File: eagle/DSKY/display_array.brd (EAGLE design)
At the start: 160 x 100 mm, 124 parts, among them IC1001 PCF8574AT, IC101 PCF8574T, IC1201 SN7400N, IC1202 SN7400N, IC1301 SN7400N, IC1302 SN7400N, IC1601 NE555V, IC201 PCF8574T, IC301 PCF8574T, IC401 PCF8574T, IC501 PCF8574T, IC601 PCF8574T, IC701 PCF8574T, IC801 PCF8574T, IC901 PCF8574AT, T1601 NX2301P, T1602 NX2301P, X1401 CLAMP_1X4-T-5MM, X1402 MALE_2X13-T-VERTICAL_2.54MM, X1501 MALE_2X13-T-VERTICAL_2.54MM

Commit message: silk screen for keys fixed
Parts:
- added LED1, LED2: red, be_opt:S_0805
- added R1: 1k5, be_rcl:S_0805
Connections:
- net N$1 renamed DRV_9_LED_R1BB
- net N$2 renamed DRV_9_LED_R1AA
- new net DRV_9_LED_R1C: LED1.C, R1.2
- new net DRV_9_LED_R1CC: LED1.A, LED2.C
- net DRV_9_LED_1: now also R1.1
- net DRV_ANODE_1: now also LED2.A
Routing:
- net DRV_9_LED_1: track 163.9 -> 213.2 mm, vias 0 -> 2
- net DRV_ANODE_1: track 244.4 -> 260.4 mm
- net DRV_9_LED_R1C: track 0.00 -> 9.71 mm
- net DRV_9_LED_R1CC: track 0.00 -> 5.07 mm

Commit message: fixed attributes
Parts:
- removed LED1, LED2: red, be_opt:S_0805
- removed R1: 1k5, be_rcl:S_0805
- added C1604: 10n, be_rcl:S_0805
- added LED912, LED913: red, be_opt:S_0805
- added R910: 2k5, be_rcl:S_0805
- C1602: value 47n -> 100n
- C1603: value 10n -> 100n
- LED903: value green -> red
- LED905: value yellow -> green
- LED907: value red -> yellow
- LED908: value blue -> red
- LED910: value red -> blue
- R903: value 750 -> 1k5
- R905: value 2k2 -> 750
- R907: value 3k3 -> 2k2
- R908: value 2k5 -> 3k3
- moved C1602 71.7 mm to (3.00, -2.00), turned to 0 degrees
- moved R903 61.7 mm to (68.0, 79.0)
- moved LED903 56.5 mm to (68.2, 86.8), turned to 90 degrees
- moved LED901 54.0 mm to (41.1, 86.8)
- moved R901 54.0 mm to (41.0, 79.0)
- moved LED910 31.3 mm to (124.0, 71.0), turned to 270 degrees
- moved LED911 27.0 mm to (41.1, 83.2)
- moved LED902 27.0 mm to (95.2, 86.8)
- moved R902 27.0 mm to (95.0, 79.0)
- moved C1603 14.1 mm to (12.8, 69.0), turned to 180 degrees
- moved R906 8.40 mm to (131.8, 62.2)
- moved LED904 4.00 mm to (124.0, 95.0)
- moved LED905 4.00 mm to (124.0, 91.0)
- moved LED906 4.00 mm to (124.0, 87.0)
- moved LED907 4.00 mm to (124.0, 83.0)
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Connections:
- new net N$1: C1602.2, C1603.1
- net DRV_9_LED_1: now also R903.1; no longer R1.1
- net DRV_9_LED_2: now also R904.1; no longer R903.1
- net DRV_9_LED_3: now also R905.1; no longer R904.1
- net DRV_9_LED_4: now also R906.1; no longer R905.1
- net DRV_9_LED_5: now also R907.1; no longer R906.1
- net DRV_9_LED_6: now also R908.1; no longer R907.1
- net DRV_9_LED_7: now also R909.1; no longer R908.1
- net DRV_9_LED_8: now also R910.1; no longer R909.1
- net DRV_9_LED_R1A: now also LED902.C, R902.2; no longer LED901.C, R901.2
- net DRV_9_LED_R1AA: now also LED902.A, LED912.C; no longer LED901.A, LED910.C
- net DRV_9_LED_R1B: now also LED903.C, R903.2; no longer LED902.C, R902.2
- net DRV_9_LED_R1BB: now also LED903.A, LED913.C; no longer LED902.A, LED911.C
- net DRV_9_LED_R1C: now also LED901.C, R901.2; no longer LED1.C, R1.2
- net DRV_9_LED_R1CC: now also LED901.A, LED911.C; no longer LED1.A, LED2.C
- net DRV_9_LED_R2: now also LED904.C, R904.2; no longer LED903.C, R903.2
- net DRV_9_LED_R3: now also LED905.C, R905.2; no longer LED904.C, R904.2
- net DRV_9_LED_R4: now also LED906.C, R906.2; no longer LED905.C, R905.2
- net DRV_9_LED_R5: now also LED907.C, R907.2; no longer LED906.C, R906.2
- net DRV_9_LED_R6: now also LED908.C, R908.2; no longer LED907.C, R907.2
- net DRV_9_LED_R7: now also LED909.C, R909.2; no longer LED908.C, R908.2
- net DRV_9_LED_R8: now also LED910.C, R910.2; no longer LED909.C, R909.2
- net DRV_ANODE_1: now also LED912.A, LED913.A; no longer LED2.A, LED903.A
- net GND: now also C1604.2; no longer C1602.2
- net TIM_1: now also C1604.1; no longer C1603.1
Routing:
- net TIM_2: track 39.3 -> 31.9 mm

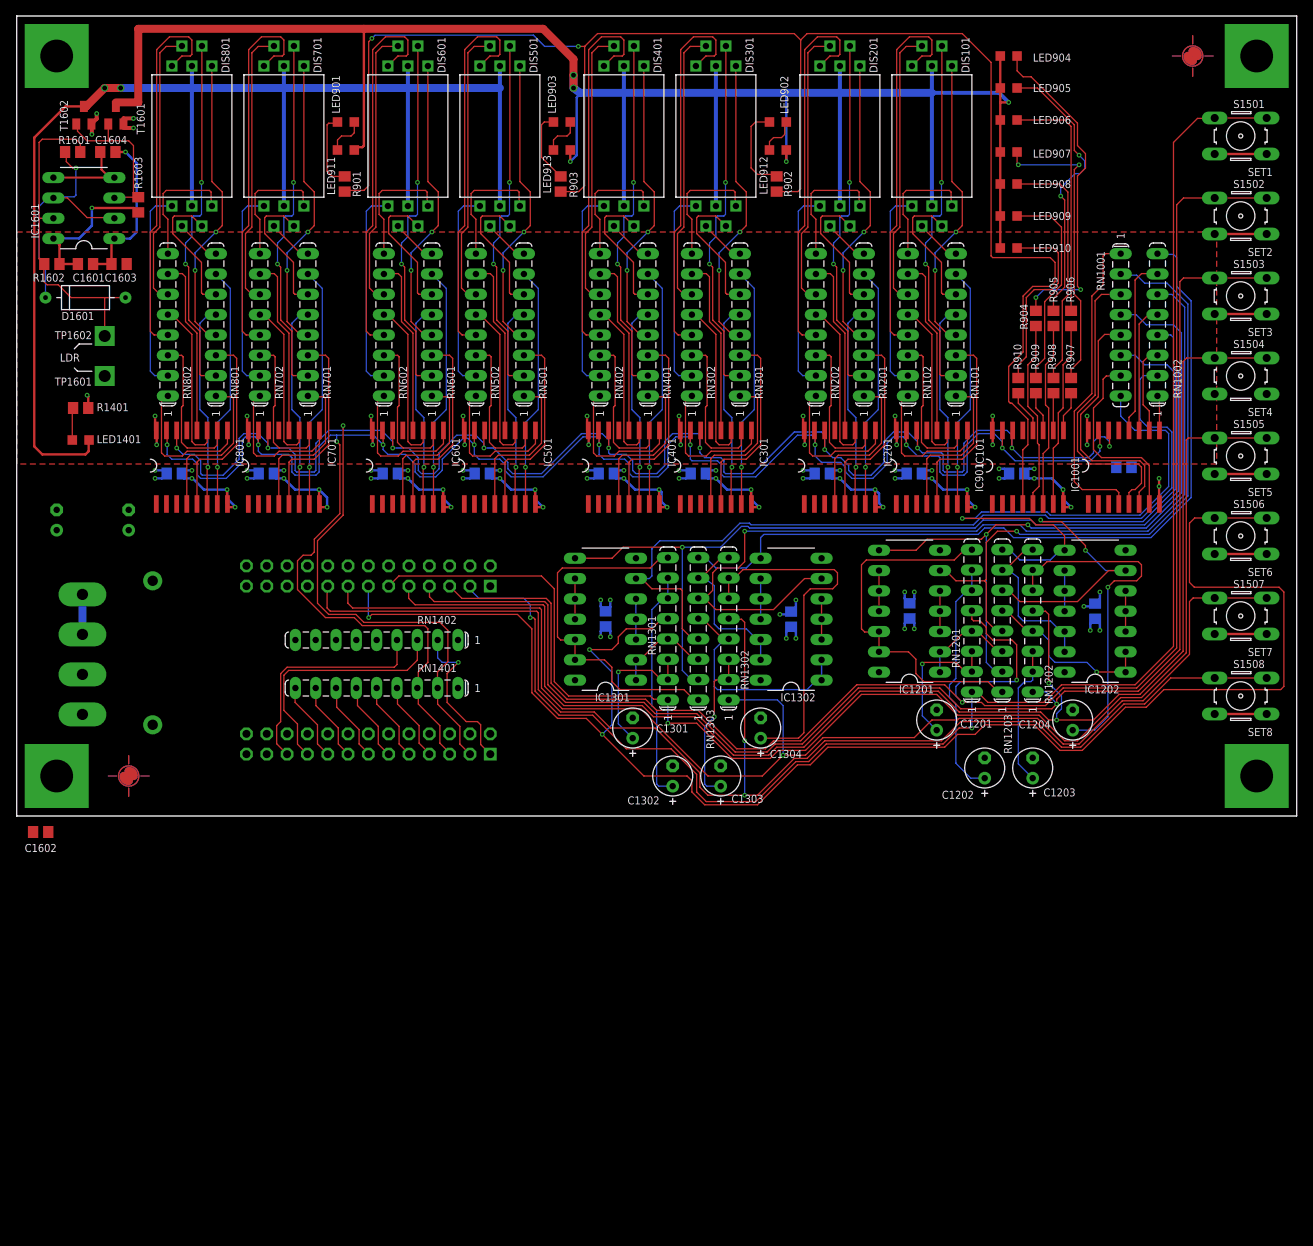
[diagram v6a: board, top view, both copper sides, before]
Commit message: -routed supply -applied dru Q-Print standard
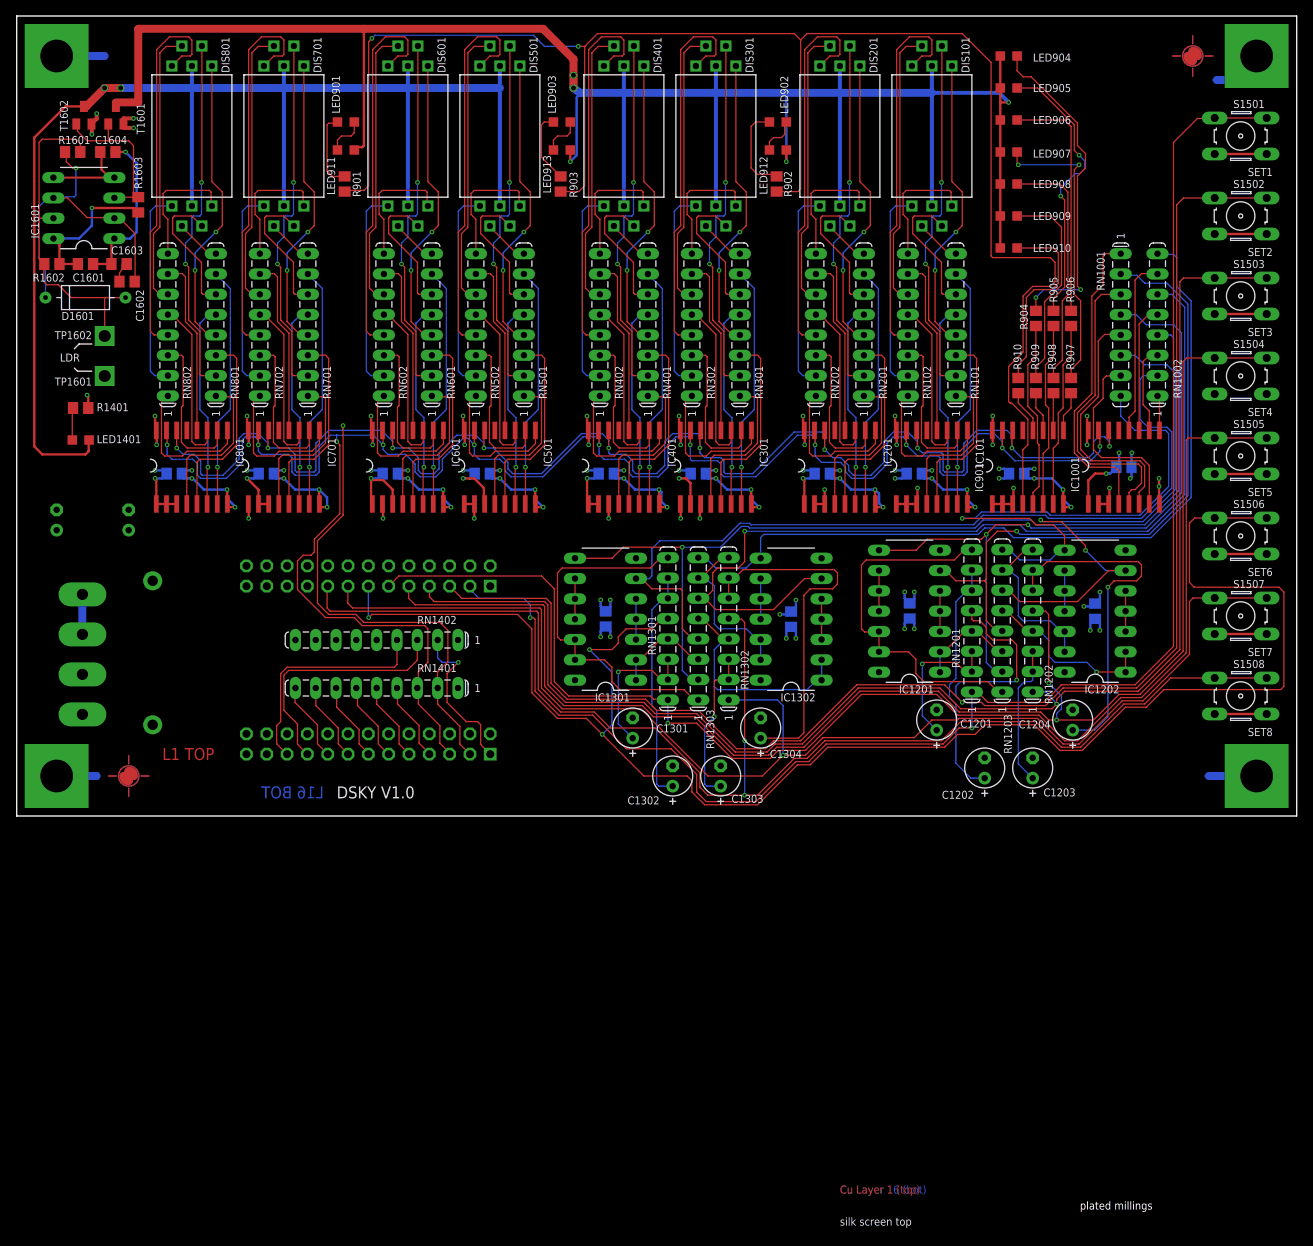
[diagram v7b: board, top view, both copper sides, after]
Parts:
- added U$1: (no value), be_frame:A4_LANDSCAPE
- R909, R910: value 2k5 -> 2k4
- moved C1602 69.6 mm to (13.8, 66.8), turned to 180 degrees
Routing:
- net GND: track 209.6 -> 263.9 mm, vias 48 -> 60
- net P5V: track 111.6 -> 157.3 mm, vias 51 -> 53
- net TIM_2: track 31.9 -> 41.3 mm
- net N$1: track 0.00 -> 2.85 mm
- net KEYPAD_1_K_1: track 39.6 -> 39.1 mm
- added copper zone on layer 15, net GND
- added copper zone on layer 2, net P5V
- removed copper zone on layer 1, net P5V
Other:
- board text added: "DSKY V1.0"
- board text added: "L1 TOP"
- board text added: "L15 GND"
- board text added: "L16 BOT"
- board text added: "L2 P5V"

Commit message: fixed silk screen issues
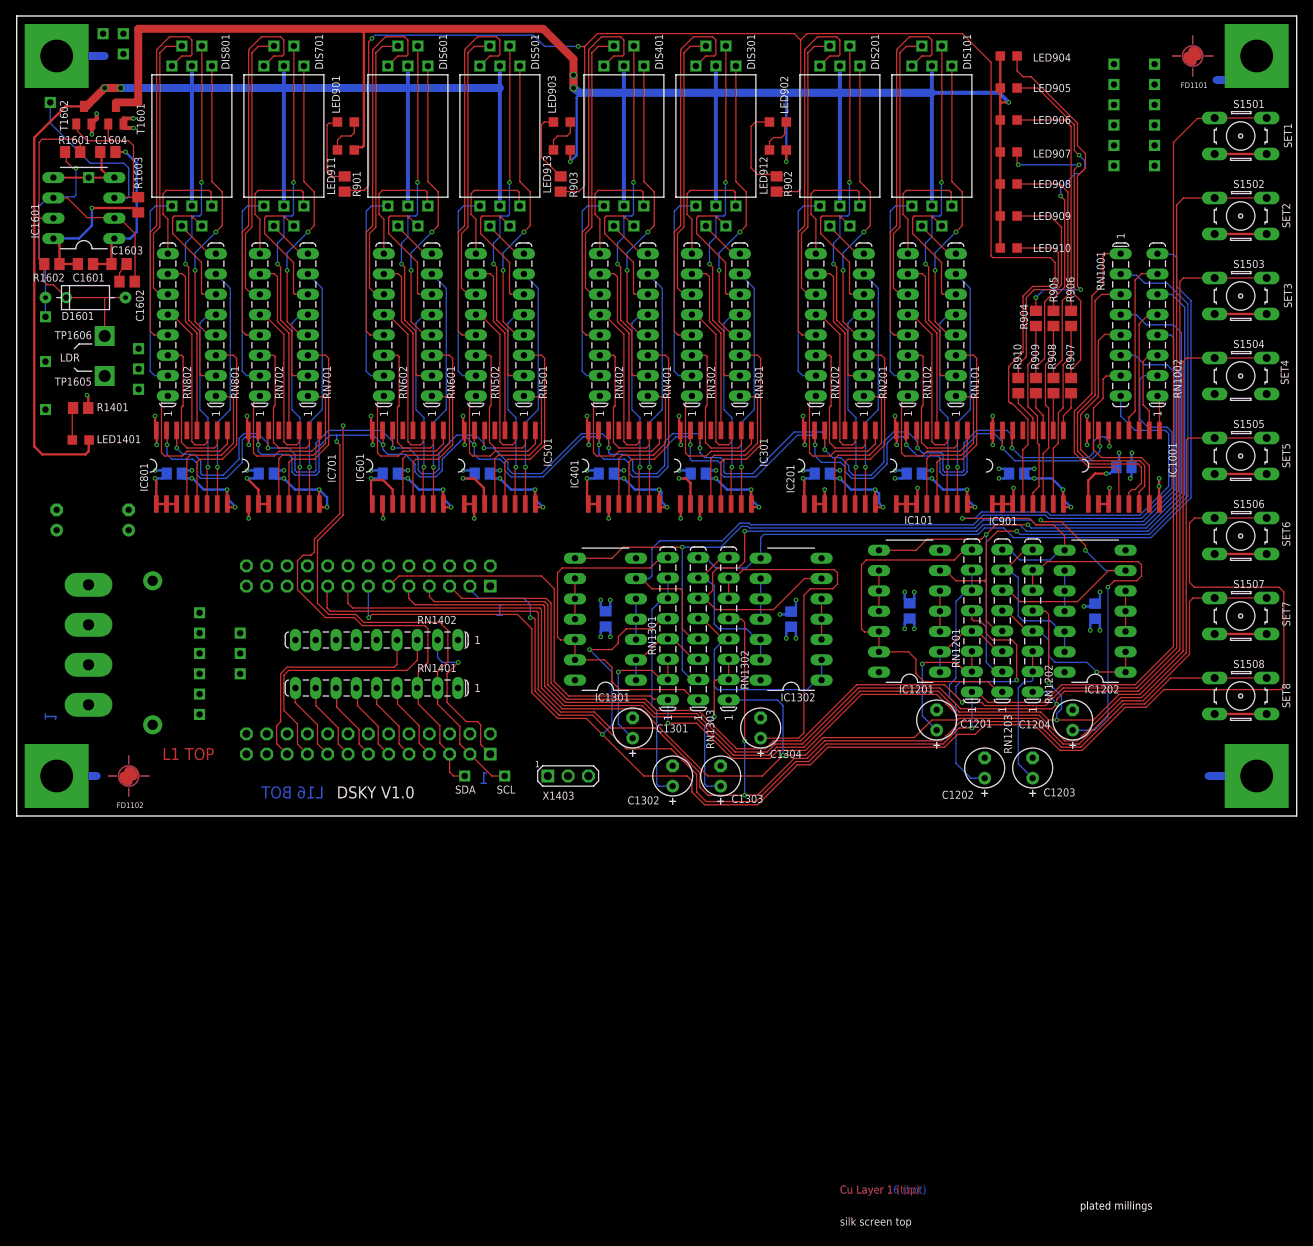
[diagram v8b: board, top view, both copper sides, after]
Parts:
- added TP1101, TP1102, TP1103, TP1104, TP1105, TP1106, TP1107, TP1108, TP1109, TP1110, TP1111, TP1112, TP1113, TP1114, TP1115, TP1116, TP1117, TP1118, TP1119, TP1120, TP1121, TP1122, TP1123, TP1124, TP1125, TP1126, TP1127, TP1401, TP1402, TP1603, TP1604, TP1607: TEST_POINT_T_SMALL, be_con_jump:T_TEST_POINT_SMALL
- added TP1605, TP1606: TEST_POINT_T_LARGE, be_con_jump:T_TEST_POINT_LARGE
- added X1403: MALE_1X3, be_con_jump:T_MALE_3X1_VERTICAL
- TP1601, TP1602: value TEST_POINT_T_LARGE -> TEST_POINT_T_SMALL; device be_con_jump:T_TEST_POINT_LARGE -> be_con_jump:T_TEST_POINT_SMALL
- moved TP1601 10.5 mm to (3.60, 62.4)
- moved TP1602 8.06 mm to (3.60, 56.8)
- moved X1401 1.44 mm to (9.00, 21.4), turned to 90 degrees
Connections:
- net N$1 renamed TIM_45
- net CTRL_SCL: now also TP1401.1
- net CTRL_SDA: now also TP1402.1
- net GND: now also TP1603.1, X1403.1
- net P5V: now also TP1602.1, TP1605.1, X1403.3; no longer TP1601.1
- net TIM_1: now also TP1604.1
- net TIM_2: now also TP1601.1
- net TIM_3: now also TP1606.1; no longer TP1602.1
- net TIM_OUT: now also TP1607.1
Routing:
- net TIM_OUT: track 20.5 -> 40.7 mm
- net CTRL_SCL: track 258.0 -> 263.4 mm
- net P5V: track 157.3 -> 152.2 mm
- net CTRL_SDA: track 252.1 -> 256.4 mm
- net TIM_2: track 41.3 -> 43.7 mm
- net TIM_3: vias 0 -> 1
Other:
- board text added: "1"
- board text added: "GND"
- board text added: "P5V"
